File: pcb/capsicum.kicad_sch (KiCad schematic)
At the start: 69 parts, among them J2 Screw_Terminal_01x02, J3 USB-C 16+8 USB 2.0, Q1 NS2101P, Q2 BC817-16LT3G, SW1 SW_SPDT, SW3 SW_SPDT, U1 ESP32-C3-WROOM-02, U2 TQ33E-1, U3 AP2112K, U4 MCP73831

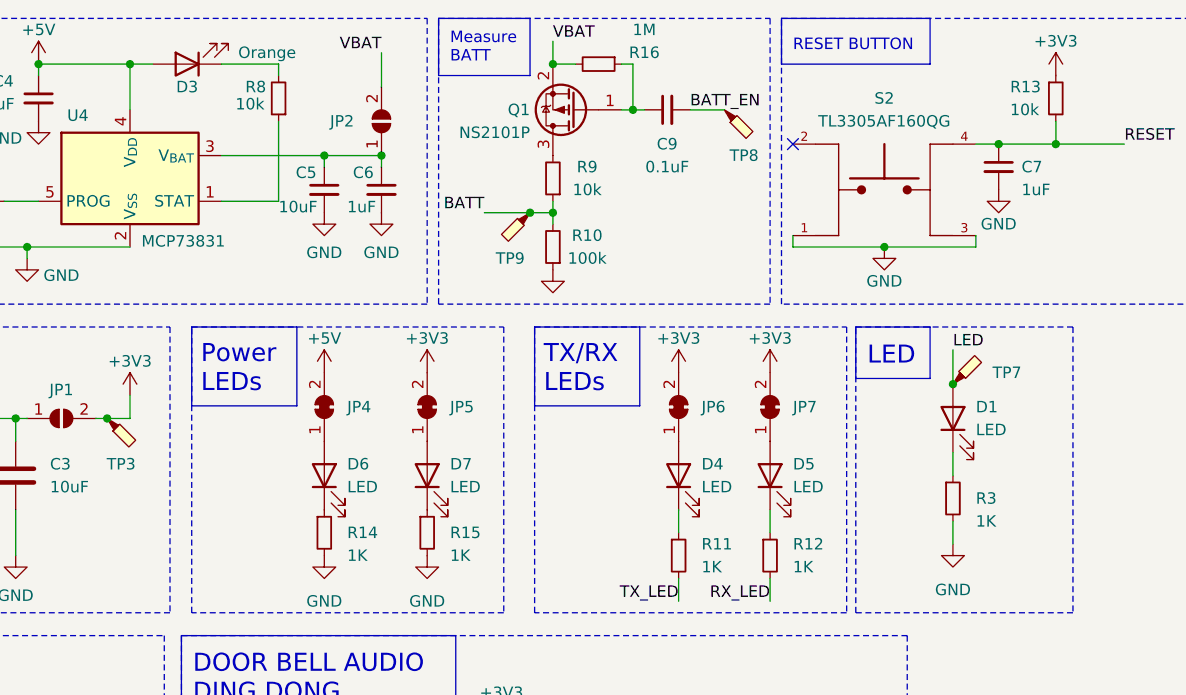
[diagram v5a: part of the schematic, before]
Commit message: feat: associate MPN and BOM details for orange LED in charging circuit
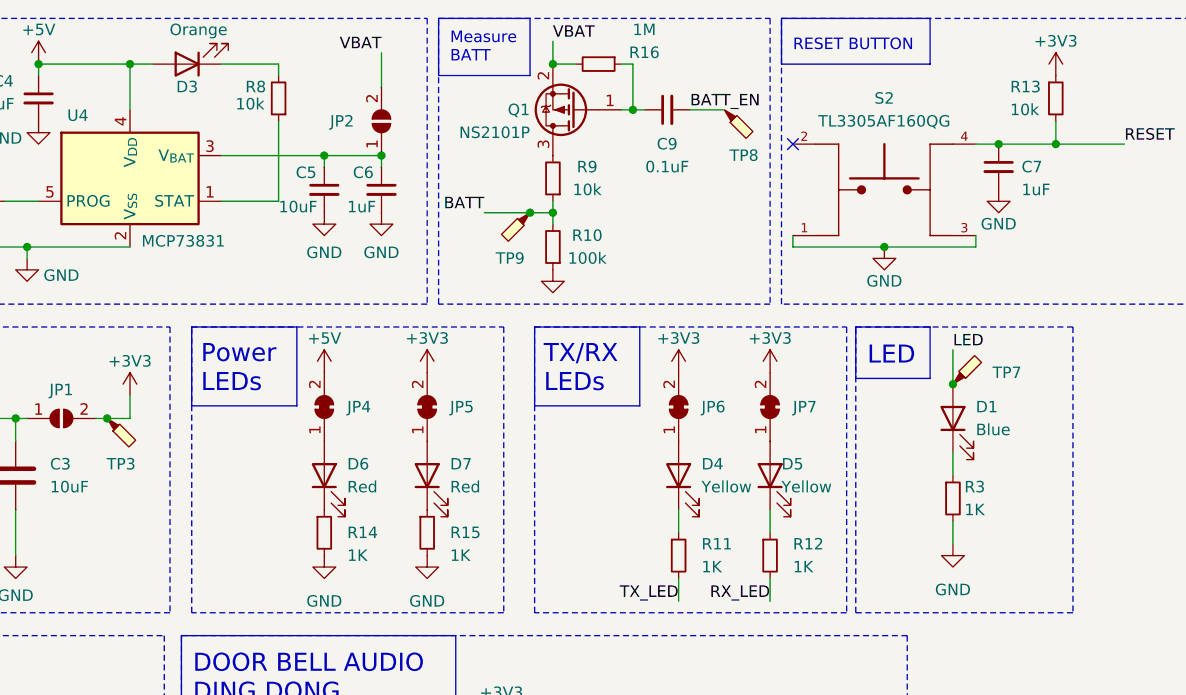
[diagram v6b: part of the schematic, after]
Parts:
- D1: value LED -> Blue; Link (none) -> https://www.pcbway.com/components/detail/150060BS75000/2916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; MANUFACTURER (none) -> Würth Elektronik; MPN (none) -> 150060BS75000; Package (none) -> 0603; Vendor (none) -> PCBWAY
- D3: Link (none) -> https://www.pcbway.com/components/detail/B1911UD20D001014U1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; MANUFACTURER (none) -> Harvatek Corporation; MPN (none) -> B1911UD--20D001014U1930; Package (none) -> 0603; Vendor (none) -> PCBWay
- D4, D5: value LED -> Yellow
- D6, D7: value LED -> Red
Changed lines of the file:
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@@
   (symbol (lib_id "Device:R_Small") (at 256.54 71.12 0) (unit 1)
     (in_bom yes) (on_board yes) (dnp no)
-    (property "Reference" "R3" (at 259.08 71.12 0)
-      (effects (font (size 1.27 1.27)) (justify left))
-    )
-    (property "Value" "1K" (at 259.08 73.66 0)
+    (property "Reference" "R3" (at 257.81 69.85 0)
+      (effects (font (size 1.27 1.27)) (justify left))
+    )
+    (property "Value" "1K" (at 257.81 72.39 0)
       (effects (font (size 1.27 1.27)) (justify left))
     )
@@
       (effects (font (size 1.27 1.27)) (justify right))
     )
-    (property "Value" "LED" (at 259.08 63.5 90)
+    (property "Value" "Blue" (at 259.08 63.5 90)
       (effects (font (size 1.27 1.27)) (justify right))
     )
@@
       (effects (font (size 1.27 1.27)) hide)
     )
-    (property "Datasheet" "~" (at 256.54 62.23 0)
-      (effects (font (size 1.27 1.27)) hide)
-    )
-    (property "Link" "" (at 256.54 62.23 0)
-      (effects (font (size 1.27 1.27)) hide)
-    )
-    (property "Vendor" "" (at 256.54 62.23 0)
-      (effects (font (size 1.27 1.27)) hide)
-    )
-    (property "MPN" "" (at 256.54 62.23 0)
-      (effects (font (size 1.27 1.27)) hide)
-    )
-    (property "Package" "" (at 256.54 62.23 0)
+    (property "Datasheet" "https://www.we-online.com/components/products/datasheet/150060BS75000.pdf" (at 256.54 62.23 0)
+      (effects (font (size 1.27 1.27)) hide)
+    )
+    (property "Link" "https://www.pcbway.com/components/detail/150060BS75000/291677/" (at 256.54 62.23 0)
+      (effects (font (size 1.27 1.27)) hide)
+    )
+    (property "Vendor" "PCBWAY" (at 256.54 62.23 0)
+      (effects (font (size 1.27 1.27)) hide)
+    )
+    (property "MPN" "150060BS75000" (at 256.54 62.23 0)
+      (effects (font (size 1.27 1.27)) hide)
+    )
+    (property "Package" "0603" (at 256.54 62.23 0)
+      (effects (font (size 1.27 1.27)) hide)
+    )
+    (property "MANUFACTURER" "Würth Elektronik" (at 256.54 62.23 0)
       (effects (font (size 1.27 1.27)) hide)
     )
@@
   (symbol (lib_id "Device:LED") (at 236.22 68.58 90) (unit 1)
     (in_bom yes) (on_board yes) (dnp no)
-    (property "Reference" "D5" (at 238.76 67.31 90)
+    (property "Reference" "D5" (at 237.49 67.31 90)
       (effects (font (size 1.27 1.27)) (justify right))
     )
-    (property "Value" "LED" (at 238.76 69.85 90)
+    (property "Value" "Yellow" (at 237.49 69.85 90)
       (effects (font (size 1.27 1.27)) (justify right))
     )
@@
       (effects (font (size 1.27 1.27)) (justify right))
     )
-    (property "Value" "LED" (at 189.23 69.85 90)
+    (property "Value" "Red" (at 189.23 69.85 90)
       (effects (font (size 1.27 1.27)) (justify right))
     )
@@
       (effects (font (size 1.27 1.27)) (justify right))
     )
-    (property "Value" "LED" (at 200.66 69.85 90)
+    (property "Value" "Red" (at 200.66 69.85 90)
       (effects (font (size 1.27 1.27)) (justify right))
     )
@@
       (effects (font (size 1.27 1.27)) (justify right))
     )
-    (property "Value" "LED" (at 228.6 69.85 90)
+    (property "Value" "Yellow" (at 228.6 69.85 90)
       (effects (font (size 1.27 1.27)) (justify right))
     )
@@
       (effects (font (size 1.27 1.27)))
     )
-    (property "Value" "Orange" (at 180.34 21.59 0)
+    (property "Value" "Orange" (at 172.72 19.05 0)
       (effects (font (size 1.27 1.27)))
     )
@@
       (effects (font (size 1.27 1.27)) hide)
     )
-    (property "Datasheet" "~" (at 171.45 22.86 0)
-      (effects (font (size 1.27 1.27)) hide)
-    )
-    (property "MPN" "" (at 171.45 22.86 0)
-      (effects (font (size 1.27 1.27)) hide)
-    )
-    (property "Package" "" (at 171.45 22.86 0)
-      (effects (font (size 1.27 1.27)) hide)
-    )
+    (property "Datasheet" "https://mm.digikey.com/Volume0/opasdata/d220001/medias/docus/3697/B1911UD--20D001014U1930.pdf" (at 171.45 22.86 0)
+      (effects (font (size 1.27 1.27)) hide)
+    )
+    (property "MPN" "B1911UD--20D001014U1930" (at 171.45 22.86 0)
+      (effects (font (size 1.27 1.27)) hide)
+    )
+    (property "Package" "0603" (at 171.45 22.86 0)
+      (effects (font (size 1.27 1.27)) hide)
+    )
+    (property "Link" "https://www.pcbway.com/components/detail/B1911UD20D001014U1930/288021/" (at 171.45 22.86 0)
+      (effects (font (size 1.27 1.27)) hide)
+    )
+    (property "MANUFACTURER" "Harvatek Corporation" (at 171.45 22.86 0)
+      (effects (font (size 1.27 1.27)) hide)
+    )
+    (property "Vendor" "PCBWay" (at 171.45 22.86 0)
+      (effects (font (size 1.27 1.27)) hide)
+    )

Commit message: feat: associate MPN and BOM details for yellow LED in charging circuit
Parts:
- D4, D5: Link (none) -> https://www.pcbway.com/components/detail/150060YS75000/2833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; MANUFACTURER (none) -> Würth Elektronik; MPN (none) -> 150060YS75000; Package (none) -> 0603; Vendor (none) -> PCBWay
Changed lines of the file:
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@@
       (effects (font (size 1.27 1.27)) hide)
     )
-    (property "Datasheet" "~" (at 236.22 68.58 0)
-      (effects (font (size 1.27 1.27)) hide)
-    )
-    (property "Link" "" (at 236.22 68.58 0)
-      (effects (font (size 1.27 1.27)) hide)
-    )
-    (property "Vendor" "" (at 236.22 68.58 0)
-      (effects (font (size 1.27 1.27)) hide)
-    )
-    (property "MPN" "" (at 236.22 68.58 0)
-      (effects (font (size 1.27 1.27)) hide)
-    )
-    (property "Package" "" (at 236.22 68.58 0)
+    (property "Datasheet" "https://www.we-online.com/components/products/datasheet/150060YS75000.pdf" (at 236.22 68.58 0)
+      (effects (font (size 1.27 1.27)) hide)
+    )
+    (property "Link" "https://www.pcbway.com/components/detail/150060YS75000/283373/" (at 236.22 68.58 0)
+      (effects (font (size 1.27 1.27)) hide)
+    )
+    (property "Vendor" "PCBWay" (at 236.22 68.58 0)
+      (effects (font (size 1.27 1.27)) hide)
+    )
+    (property "MPN" "150060YS75000" (at 236.22 68.58 0)
+      (effects (font (size 1.27 1.27)) hide)
+    )
+    (property "Package" "0603" (at 236.22 68.58 0)
+      (effects (font (size 1.27 1.27)) hide)
+    )
+    (property "MANUFACTURER" "Würth Elektronik" (at 236.22 68.58 0)
       (effects (font (size 1.27 1.27)) hide)
     )
@@
       (effects (font (size 1.27 1.27)) hide)
     )
-    (property "Datasheet" "~" (at 226.06 68.58 0)
-      (effects (font (size 1.27 1.27)) hide)
-    )
-    (property "Link" "" (at 226.06 68.58 0)
-      (effects (font (size 1.27 1.27)) hide)
-    )
-    (property "Vendor" "" (at 226.06 68.58 0)
-      (effects (font (size 1.27 1.27)) hide)
-    )
-    (property "MPN" "" (at 226.06 68.58 0)
-      (effects (font (size 1.27 1.27)) hide)
-    )
-    (property "Package" "" (at 226.06 68.58 0)
-      (effects (font (size 1.27 1.27)) hide)
-    )
+    (property "Datasheet" "https://www.we-online.com/components/products/datasheet/150060YS75000.pdf" (at 226.06 68.58 0)
+      (effects (font (size 1.27 1.27)) hide)
+    )
+    (property "Link" "https://www.pcbway.com/components/detail/150060YS75000/283373/" (at 226.06 68.58 0)
+      (effects (font (size 1.27 1.27)) hide)
+    )
+    (property "Vendor" "PCBWay" (at 226.06 68.58 0)
+      (effects (font (size 1.27 1.27)) hide)
+    )
+    (property "MPN" "150060YS75000" (at 226.06 68.58 0)
+      (effects (font (size 1.27 1.27)) hide)
+    )
+    (property "Package" "0603" (at 226.06 68.58 0)
+      (effects (font (size 1.27 1.27)) hide)
+    )
+    (property "MANUFACTURER" "Würth Elektronik" (at 226.06 68.58 0)
+      (effects (font (size 1.27 1.27)) hide)
+    )

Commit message: feat: associate MPN and BOM details for red LED in charging circuit
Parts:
- D6, D7: Link (none) -> https://www.pcbway.com/components/detail/150060RS75000/2916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; MANUFACTURER (none) -> Würth Elektronik; MPN (none) -> 150060RS75000; Package (none) -> 0603; Vendor (none) -> PCBWay
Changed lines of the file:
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@@
       (effects (font (size 1.27 1.27)) hide)
     )
-    (property "Datasheet" "~" (at 186.69 68.58 0)
+    (property "Datasheet" "https://www.we-online.com/components/products/datasheet/150060RS75000.pdf" (at 186.69 68.58 0)
       (effects (font (size 1.27 1.27)) hide)
     )
-    (property "Link" "" (at 186.69 68.58 0)
+    (property "Link" "https://www.pcbway.com/components/detail/150060RS75000/291675/" (at 186.69 68.58 0)
       (effects (font (size 1.27 1.27)) hide)
     )
-    (property "Vendor" "" (at 186.69 68.58 0)
+    (property "Vendor" "PCBWay" (at 186.69 68.58 0)
       (effects (font (size 1.27 1.27)) hide)
     )
-    (property "MPN" "" (at 186.69 68.58 0)
+    (property "MPN" "150060RS75000" (at 186.69 68.58 0)
       (effects (font (size 1.27 1.27)) hide)
     )
-    (property "Package" "" (at 186.69 68.58 0)
+    (property "Package" "0603" (at 186.69 68.58 0)
+      (effects (font (size 1.27 1.27)) hide)
+    )
+    (property "MANUFACTURER" "Würth Elektronik" (at 186.69 68.58 0)
       (effects (font (size 1.27 1.27)) hide)
     )
@@
       (effects (font (size 1.27 1.27)) hide)
     )
-    (property "Datasheet" "~" (at 198.12 68.58 0)
+    (property "Datasheet" "https://www.we-online.com/components/products/datasheet/150060RS75000.pdf" (at 198.12 68.58 0)
       (effects (font (size 1.27 1.27)) hide)
     )
-    (property "Link" "" (at 198.12 68.58 0)
+    (property "Link" "https://www.pcbway.com/components/detail/150060RS75000/291675/" (at 198.12 68.58 0)
       (effects (font (size 1.27 1.27)) hide)
     )
-    (property "Vendor" "" (at 198.12 68.58 0)
+    (property "Vendor" "PCBWay" (at 198.12 68.58 0)
       (effects (font (size 1.27 1.27)) hide)
     )
-    (property "MPN" "" (at 198.12 68.58 0)
+    (property "MPN" "150060RS75000" (at 198.12 68.58 0)
       (effects (font (size 1.27 1.27)) hide)
     )
-    (property "Package" "" (at 198.12 68.58 0)
+    (property "Package" "0603" (at 198.12 68.58 0)
       (effects (font (size 1.27 1.27)) hide)
     )
+    (property "MANUFACTURER" "Würth Elektronik" (at 198.12 68.58 0)
+      (effects (font (size 1.27 1.27)) hide)
+    )
